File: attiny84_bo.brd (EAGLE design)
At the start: 36 x 20 mm, 9 parts, among them J1 AVR_SPI_PRG_6NS, Y1 16MHz

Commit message: routed
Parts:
- added H1, H2: MOUNT-PAD-ROUND3.0, holes:3,0-PAD
- moved C2 1.61 mm to (30.1, 3.94), turned to 0 degrees
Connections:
- net GND: now also H1.B3,0, H2.B3,0
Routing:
- net +5V: track 0.00 -> 38.3 mm, vias 0 -> 1
- net PB0/XTAL1: track 0.00 -> 24.9 mm, vias 0 -> 1
- net N$1: track 0.00 -> 21.9 mm
- net PB1/XTAL2: track 0.00 -> 20.9 mm, vias 0 -> 1
- net PA6/MOSI: track 0.00 -> 15.8 mm
- net N$6: track 0.00 -> 12.9 mm
- net PA4/SCL: track 0.00 -> 11.7 mm
- net PB3/RESET-: track 0.00 -> 11.6 mm
- net PA5/MISO: track 0.00 -> 7.83 mm
- net N$5: track 0.00 -> 6.40 mm
- net N$4: track 0.00 -> 4.49 mm
- net N$3: track 0.00 -> 3.98 mm
- net N$2: track 0.00 -> 3.68 mm

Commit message: signal names
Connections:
- net N$1 renamed PA7
- net N$2 renamed PA3
- net N$3 renamed PA2
- net N$4 renamed PA1
- net N$5 renamed PA0
- net N$6 renamed PB2
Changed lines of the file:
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@@
 <wire x1="17.8816" y1="10.4648" x2="17.907" y2="10.408" width="0.1524" layer="1"/>
 </signal>
-<signal name="N$1">
+<signal name="PA7">
 <contactref element="U$1" pad="6"/>
 <contactref element="JP1" pad="15"/>
@@
 <wire x1="8.7376" y1="6.9088" x2="8.763" y2="6.858" width="0.1524" layer="1"/>
 </signal>
-<signal name="N$2">
+<signal name="PA3">
 <contactref element="U$1" pad="10"/>
 <contactref element="JP1" pad="7"/>
@@
 <wire x1="18.9992" y1="6.9088" x2="18.923" y2="6.858" width="0.1524" layer="1"/>
 </signal>
-<signal name="N$3">
+<signal name="PA2">
 <contactref element="U$1" pad="11"/>
 <contactref element="JP1" pad="5"/>
@@
 <wire x1="21.4376" y1="6.9088" x2="21.463" y2="6.858" width="0.1524" layer="1"/>
 </signal>
-<signal name="N$4">
+<signal name="PA1">
 <contactref element="U$1" pad="12"/>
 <contactref element="JP1" pad="3"/>
@@
 <wire x1="23.9776" y1="6.9088" x2="24.003" y2="6.858" width="0.1524" layer="1"/>
 </signal>
-<signal name="N$5">
+<signal name="PA0">
 <contactref element="U$1" pad="13"/>
 <contactref element="JP1" pad="1"/>
@@
 <wire x1="26.5176" y1="6.9088" x2="26.543" y2="6.858" width="0.1524" layer="1"/>
 </signal>
-<signal name="N$6">
+<signal name="PB2">
 <contactref element="U$1" pad="5"/>
 <contactref element="JP1" pad="10"/>

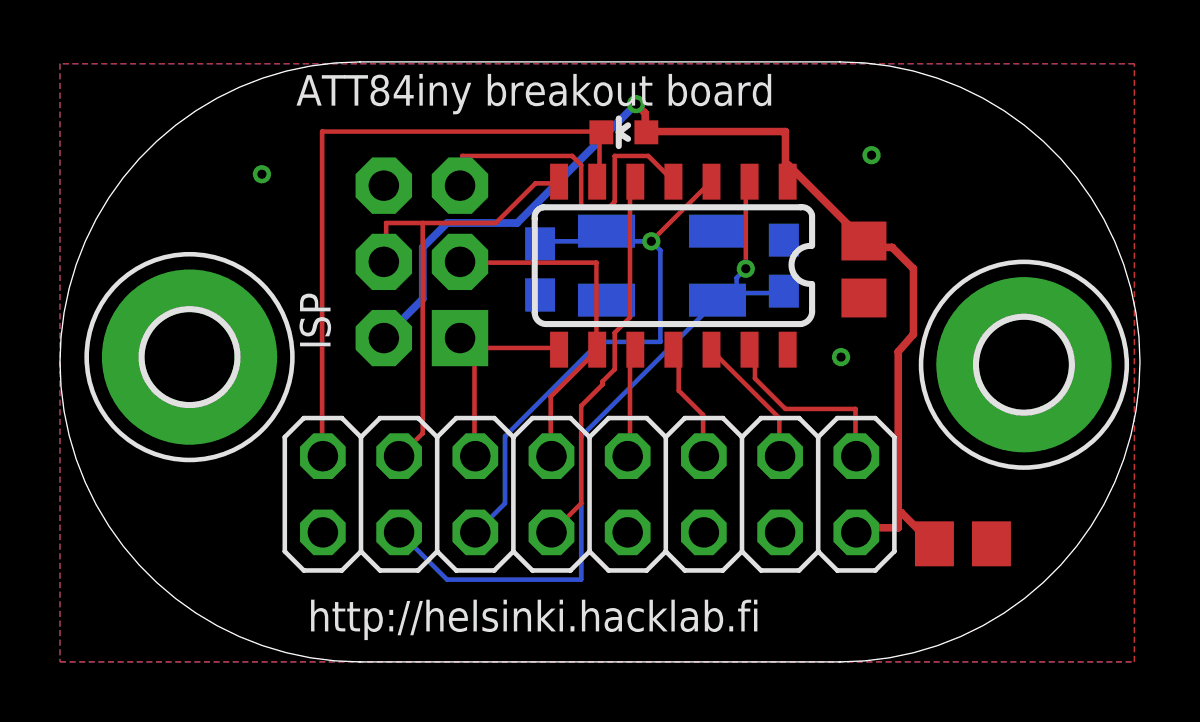
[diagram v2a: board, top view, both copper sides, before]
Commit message: second 5v input
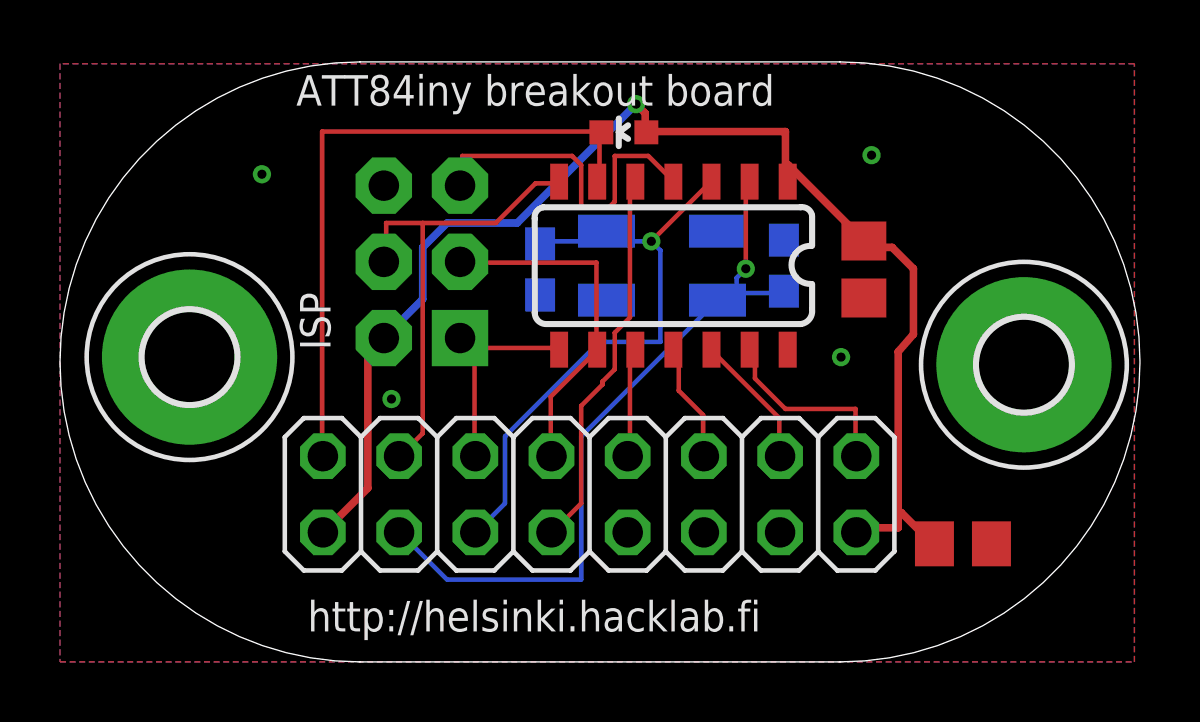
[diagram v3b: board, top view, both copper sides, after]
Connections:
- net +5V: now also JP1.16
- net GND: no longer JP1.16
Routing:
- net +5V: track 38.3 -> 45.6 mm
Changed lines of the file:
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@@
 <contactref element="C2" pad="2"/>
 <contactref element="U$1" pad="14"/>
-<contactref element="JP1" pad="16"/>
 <contactref element="JP1" pad="4"/>
 <contactref element="JP1" pad="8"/>
@@
 <contactref element="H1" pad="B3,0"/>
 <contactref element="H2" pad="B3,0"/>
+<via x="11.049" y="8.763" extent="1-16" drill="0.3048"/>
 </signal>
 <signal name="+5V" class="1">
@@
 <wire x1="29.0576" y1="3.9624" x2="29.149" y2="3.937" width="0.254" layer="1"/>
 <wire x1="28.0416" y1="4.9784" x2="27.94" y2="4.9784" width="0.254" layer="1"/>
+<contactref element="JP1" pad="16"/>
+<wire x1="10.2616" y1="5.7912" x2="8.8392" y2="4.3688" width="0.254" layer="1"/>
+<wire x1="10.2616" y1="10.2616" x2="10.2616" y2="5.7912" width="0.254" layer="1"/>
+<wire x1="10.795" y1="10.795" x2="10.2616" y2="10.2616" width="0.254" layer="1"/>
+<wire x1="8.8392" y1="4.3688" x2="8.763" y2="4.318" width="0.254" layer="1"/>
 </signal>
 <signal name="PB0/XTAL1">
